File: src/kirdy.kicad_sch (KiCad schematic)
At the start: 18 parts, among them J1 BG050-10A-0-0650-0737-0350-L-D, J2 BG050-10A-0-0650-0737-0350-L-D, J3 Kirdy LD Adapter

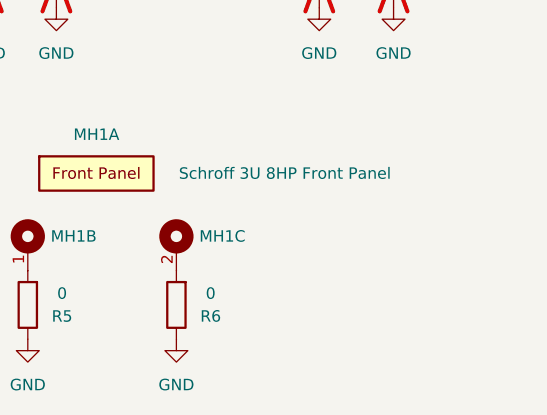
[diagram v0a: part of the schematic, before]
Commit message: sch: Add SMA Jack to Plug Cable to BOM - Internal SMA cable connecting LD adapter and Front Panel
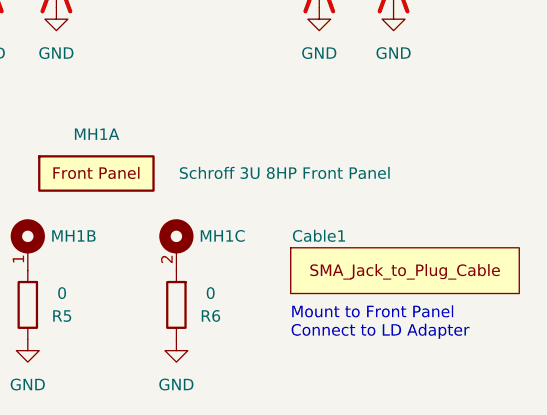
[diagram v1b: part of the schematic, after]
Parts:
- added Cable1: SMA_Jack_to_Plug_Cable, symbol kirdy:SMA_Jack_to_Plug_Cable
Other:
- note added: "Mount to Front Panel Connect to LD Adapter"
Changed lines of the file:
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@@
     (stroke (width 0) (type default))
+  )
+  (text "Mount to Front Panel \nConnect to LD Adapter" (at 322.58 219.71 0)
+    (effects (font (size 1.27 1.27)) (justify left bottom))
   )
   (text "Connectors Mating Combination:\n\nTotal Mating Height = 11mm\n\nMale: BG050-10A-0-0650-0737-0350-L-D (3.5mm profile) \nFemale: M20-7870542 (7.5mm profile) \nM3 Solder Standoff: 78614110360 (11mm height)"
@@
         )
       )
+    )
+  )
+  (symbol (lib_id "kirdy:SMA_Jack_to_Plug_Cable") (at 322.58 209.55 0) (unit 1)
+    (in_bom yes) (on_board no) (dnp no)
+    (property "Reference" "Cable1" (at 325.755 208.28 0)
+      (effects (font (size 1.27 1.27)))
+    )
+    (property "Value" "SMA_Jack_to_Plug_Cable" (at 322.58 209.55 0)
+      (effects (font (size 1.27 1.27)) hide)
+    )
+    (property "Footprint" "" (at 322.58 209.55 0)
+      (effects (font (size 1.27 1.27)) hide)
+    )
+    (property "Datasheet" "" (at 322.58 209.55 0)
+      (effects (font (size 1.27 1.27)) hide)
+    )
+    (property "MFR_PN" "095-902-477-006" (at 322.58 209.55 0)
+      (effects (font (size 1.27 1.27)) hide)
+    )
+    (property "MFR_PN_ALT" "095-902-481-006" (at 322.58 209.55 0)
+      (effects (font (size 1.27 1.27)) hide)
+    )
+    (property "Comment" "Minimum Length of Cable: 120mm" (at 322.58 209.55 0)
+      (effects (font (size 1.27 1.27)) hide)
+    )
+    (instances
+      (project "kirdy"
+        (path "/88da1dd8-9274-4b55-84fb-90006c9b6e8f"
+          (reference "Cable1") (unit 1)
+        )
+      )

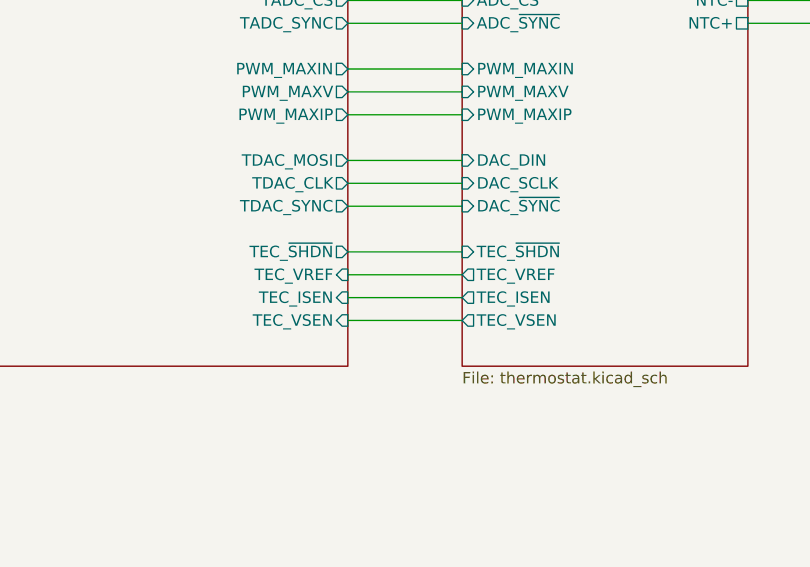
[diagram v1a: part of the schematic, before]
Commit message: sch, pcb: Add TDAC_VFB. Change 2u2 PMLCAP P/N - Connect TDAC voltage output through a RC LPF to MCU PC0(ADC123_IN10) - 2u2 PMLCAP P/N is changed to 16V version instead of 35V for lower cost
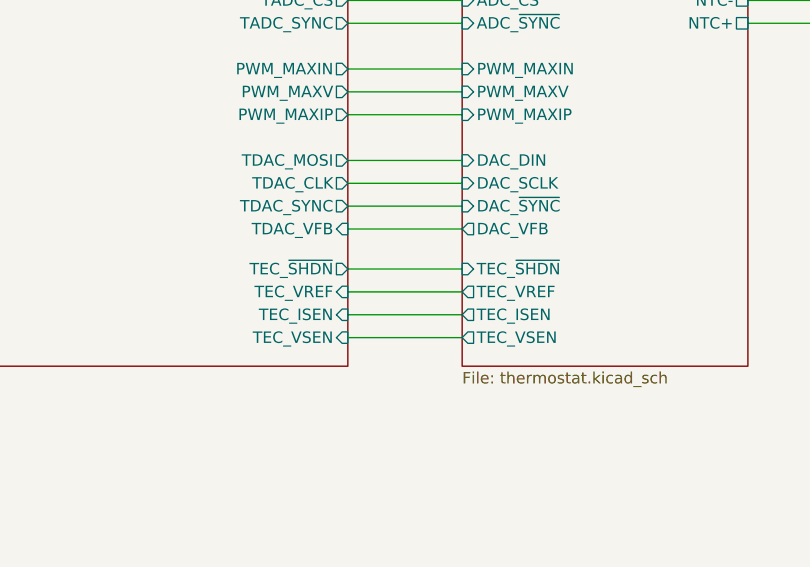
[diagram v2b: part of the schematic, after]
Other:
- sheet MCU ports: added TDAC_VFB; removed none
- sheet thermostat ports: added DAC_VFB; removed none
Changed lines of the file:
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@@
     (stroke (width 0) (type default))
   )
-  (wire (pts (xy 218.44 194.31) (xy 231.14 194.31))
+  (wire (pts (xy 218.44 196.215) (xy 231.14 196.215))
     (stroke (width 0) (type default))
   )
@@
     (stroke (width 0) (type default))
   )
-  (wire (pts (xy 218.44 189.23) (xy 231.14 189.23))
+  (wire (pts (xy 218.44 184.15) (xy 231.14 184.15))
+    (stroke (width 0) (type default))
+  )
+  (wire (pts (xy 218.44 191.135) (xy 231.14 191.135))
     (stroke (width 0) (type default))
   )
@@
     (stroke (width 0) (type default))
   )
-  (wire (pts (xy 218.44 186.69) (xy 231.14 186.69))
+  (wire (pts (xy 218.44 188.595) (xy 231.14 188.595))
     (stroke (width 0) (type default))
   )
@@
     (stroke (width 0) (type default))
   )
-  (wire (pts (xy 218.44 191.77) (xy 231.14 191.77))
+  (wire (pts (xy 218.44 193.675) (xy 231.14 193.675))
     (stroke (width 0) (type default))
   )
@@
       (effects (font (size 1.27 1.27)) (justify left))
     )
-    (pin "TEC_~{SHDN}" input (at 231.14 186.69 180)
-      (effects (font (size 1.27 1.27)) (justify left))
-    )
-    (pin "TEC_ISEN" output (at 231.14 191.77 180)
-      (effects (font (size 1.27 1.27)) (justify left))
-    )
-    (pin "TEC_VREF" output (at 231.14 189.23 180)
-      (effects (font (size 1.27 1.27)) (justify left))
-    )
-    (pin "TEC_VSEN" output (at 231.14 194.31 180)
+    (pin "TEC_~{SHDN}" input (at 231.14 188.595 180)
+      (effects (font (size 1.27 1.27)) (justify left))
+    )
+    (pin "TEC_ISEN" output (at 231.14 193.675 180)
+      (effects (font (size 1.27 1.27)) (justify left))
+    )
+    (pin "TEC_VREF" output (at 231.14 191.135 180)
+      (effects (font (size 1.27 1.27)) (justify left))
+    )
+    (pin "TEC_VSEN" output (at 231.14 196.215 180)
+      (effects (font (size 1.27 1.27)) (justify left))
+    )
+    (pin "DAC_VFB" output (at 231.14 184.15 180)
       (effects (font (size 1.27 1.27)) (justify left))
     )
@@
       (effects (font (size 1.27 1.27)) (justify right))
     )
-    (pin "TEC_~{SHDN}" output (at 218.44 186.69 0)
-      (effects (font (size 1.27 1.27)) (justify right))
-    )
-    (pin "TEC_VREF" input (at 218.44 189.23 0)
+    (pin "TEC_~{SHDN}" output (at 218.44 188.595 0)
+      (effects (font (size 1.27 1.27)) (justify right))
+    )
+    (pin "TEC_VREF" input (at 218.44 191.135 0)
       (effects (font (size 1.27 1.27)) (justify right))
     )
@@
       (effects (font (size 1.27 1.27)) (justify left))
     )
-    (pin "TEC_ISEN" input (at 218.44 191.77 0)
-      (effects (font (size 1.27 1.27)) (justify right))
-    )
-    (pin "TEC_VSEN" input (at 218.44 194.31 0)
+    (pin "TEC_ISEN" input (at 218.44 193.675 0)
+      (effects (font (size 1.27 1.27)) (justify right))
+    )
+    (pin "TEC_VSEN" input (at 218.44 196.215 0)
       (effects (font (size 1.27 1.27)) (justify right))
     )
@@
       (effects (font (size 1.27 1.27)) (justify right))
     )
+    (pin "TDAC_VFB" input (at 218.44 184.15 0)
+      (effects (font (size 1.27 1.27)) (justify right))
+    )

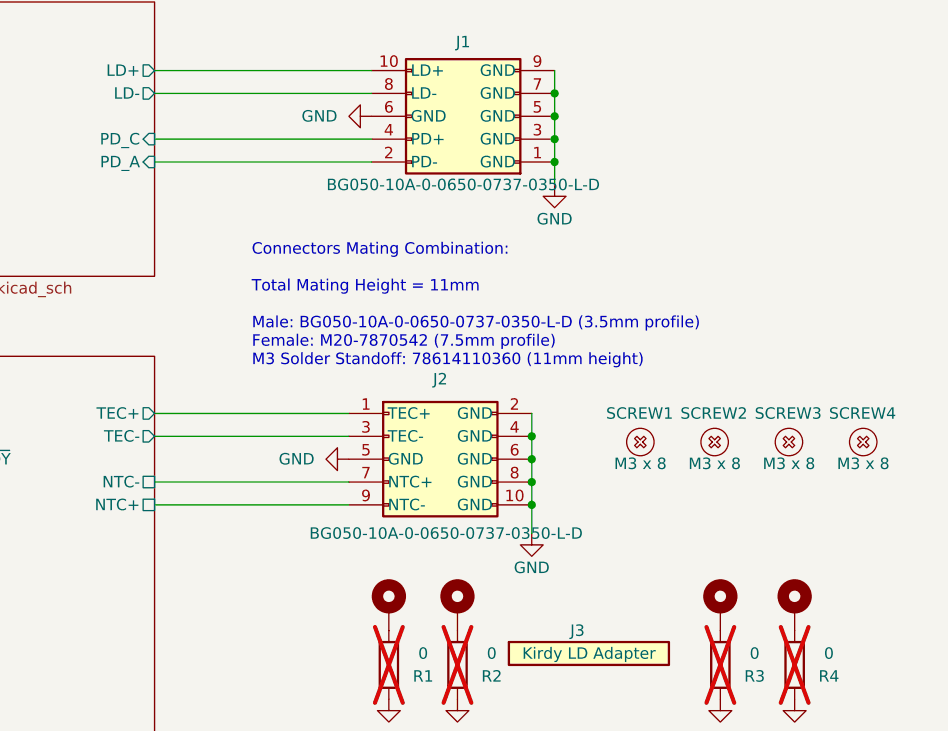
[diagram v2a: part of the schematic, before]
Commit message: sch: Add M3 Washer to BOM
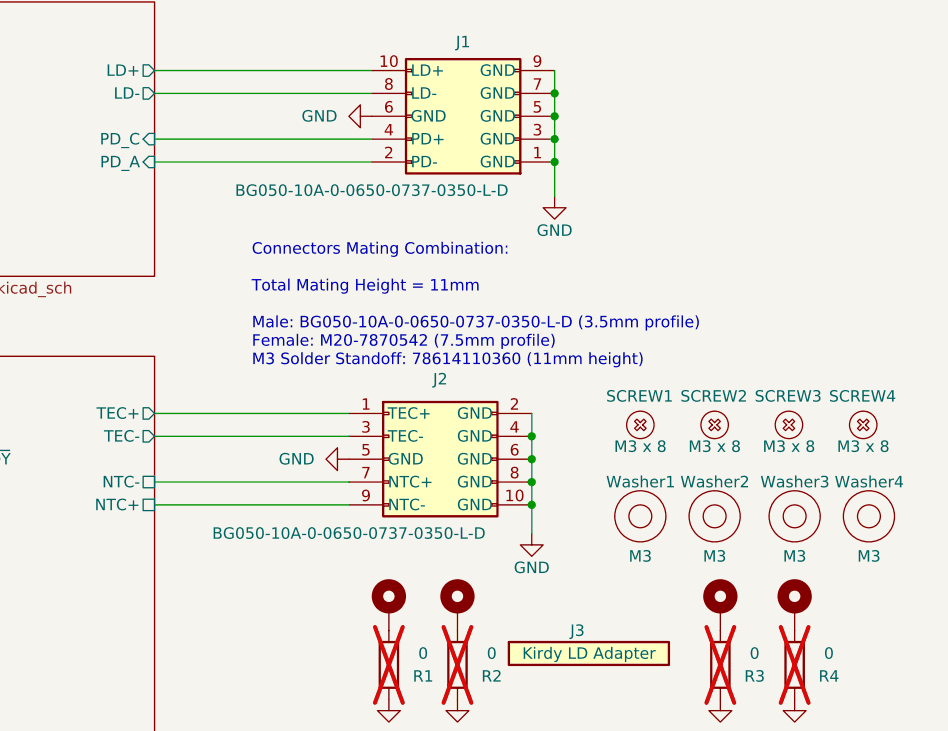
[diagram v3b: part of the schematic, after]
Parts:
- added Washer1, Washer2, Washer3, Washer4: M3, symbol kirdy:Washer
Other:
- moved on the sheet: SCREW1, SCREW2, SCREW3, SCREW4

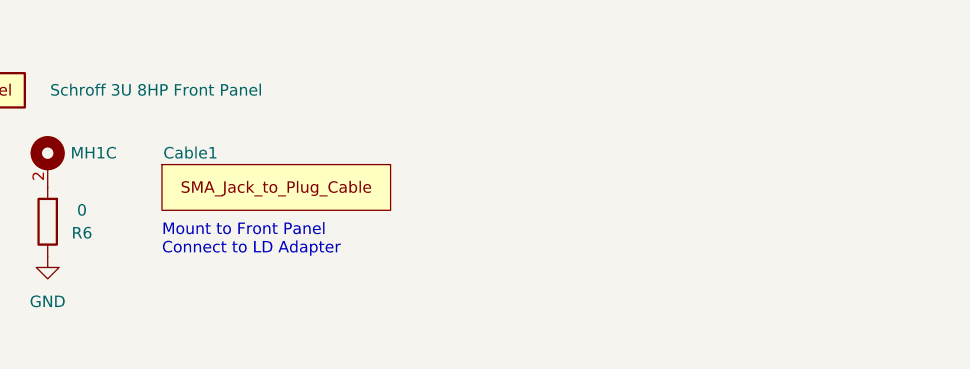
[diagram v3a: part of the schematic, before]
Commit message: bom: update MFR_PN and descriptions of SMA Cable
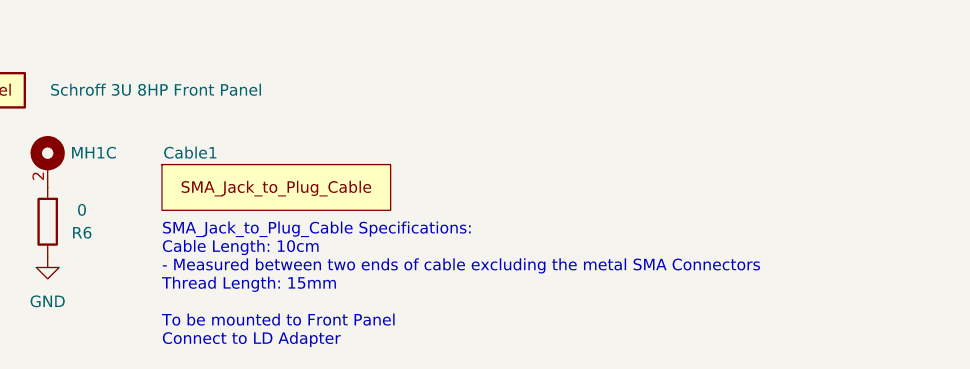
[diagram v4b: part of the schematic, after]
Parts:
- Cable1: Comment Minimum Length of Cable: 120mm -> Order from Taobao | Cable Length: 10cm | Thread Length: 15m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; MFR_PN 095-902-477-006 -> https://m.tb.cn/h.5HEJkaC?tk=6UH5WQTrLMA; MFR_PN_ALT 095-902-481-006 -> (none)
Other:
- note added: "SMA_Jack_to_Plug_Cable Specifications: Cable Length: 10cm - Measured between two ends of cable excluding the metal SMA Connectors Thread Length: 15mm To be mounted to Front Panel Connect to LD Adapter"
- note removed: "Mount to Front Panel Connect to LD Adapter"
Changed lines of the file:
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@@
     (stroke (width 0) (type default))
   )
-  (text "Mount to Front Panel \nConnect to LD Adapter" (at 322.58 219.71 0)
+  (text "SMA_Jack_to_Plug_Cable Specifications:\nCable Length: 10cm\n- Measured between two ends of cable excluding the metal SMA Connectors\nThread Length: 15mm\n\nTo be mounted to Front Panel \nConnect to LD Adapter"
+    (at 322.58 229.87 0)
     (effects (font (size 1.27 1.27)) (justify left bottom))
   )
@@
       (effects (font (size 1.27 1.27)) hide)
     )
-    (property "MFR_PN" "095-902-477-006" (at 322.58 209.55 0)
-      (effects (font (size 1.27 1.27)) hide)
-    )
-    (property "MFR_PN_ALT" "095-902-481-006" (at 322.58 209.55 0)
-      (effects (font (size 1.27 1.27)) hide)
-    )
-    (property "Comment" "Minimum Length of Cable: 120mm" (at 322.58 209.55 0)
-      (effects (font (size 1.27 1.27)) hide)
-    )
+    (property "MFR_PN" "https://m.tb.cn/h.5HEJkaC?tk=6UH5WQTrLMA" (at 322.58 209.55 0)
+      (effects (font (size 1.27 1.27)) hide)
+    )
+    (property "MFR_PN_ALT" "" (at 322.58 209.55 0)
+      (effects (font (size 1.27 1.27)) hide)
+    )
+    (property "Comment" "Order from Taobao | Cable Length: 10cm | Thread Length: 15mm | F-Type" (at 322.58 209.55 0)
+      (effects (font (size 1.27 1.27)) hide)
+    )

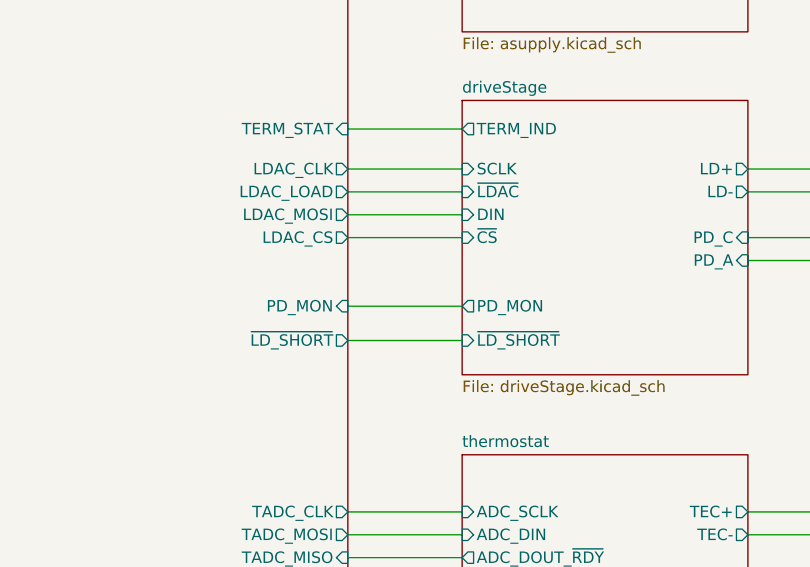
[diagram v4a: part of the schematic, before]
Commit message: Fix issiues from lis, see bug/issiue list in DOC directory
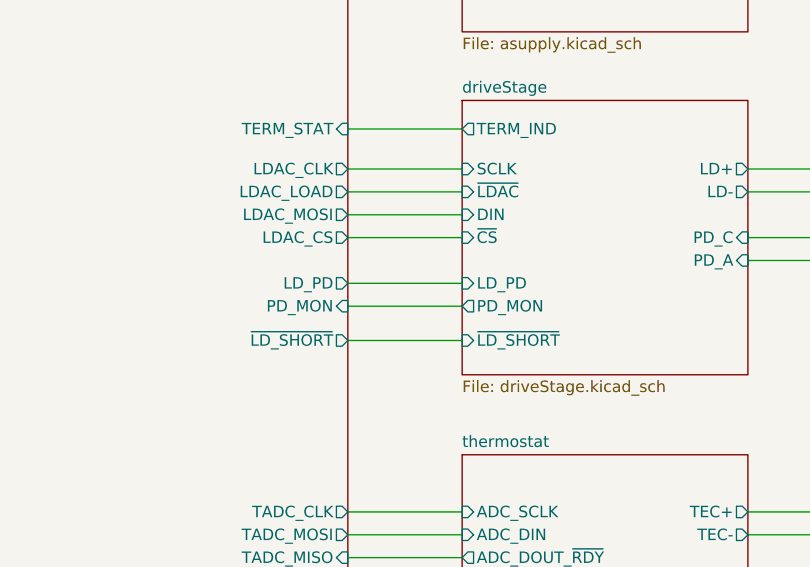
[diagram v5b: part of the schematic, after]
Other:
- sheet MCU ports: added LD_PD; removed none
- sheet driveStage ports: added LD_PD; removed none
